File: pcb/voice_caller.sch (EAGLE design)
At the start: 28 parts, among them IC1 PRO_MICRO, IC2 AT45DB321D-S, IC3 78L12SMD, K1 TQ2SA-L2-5V

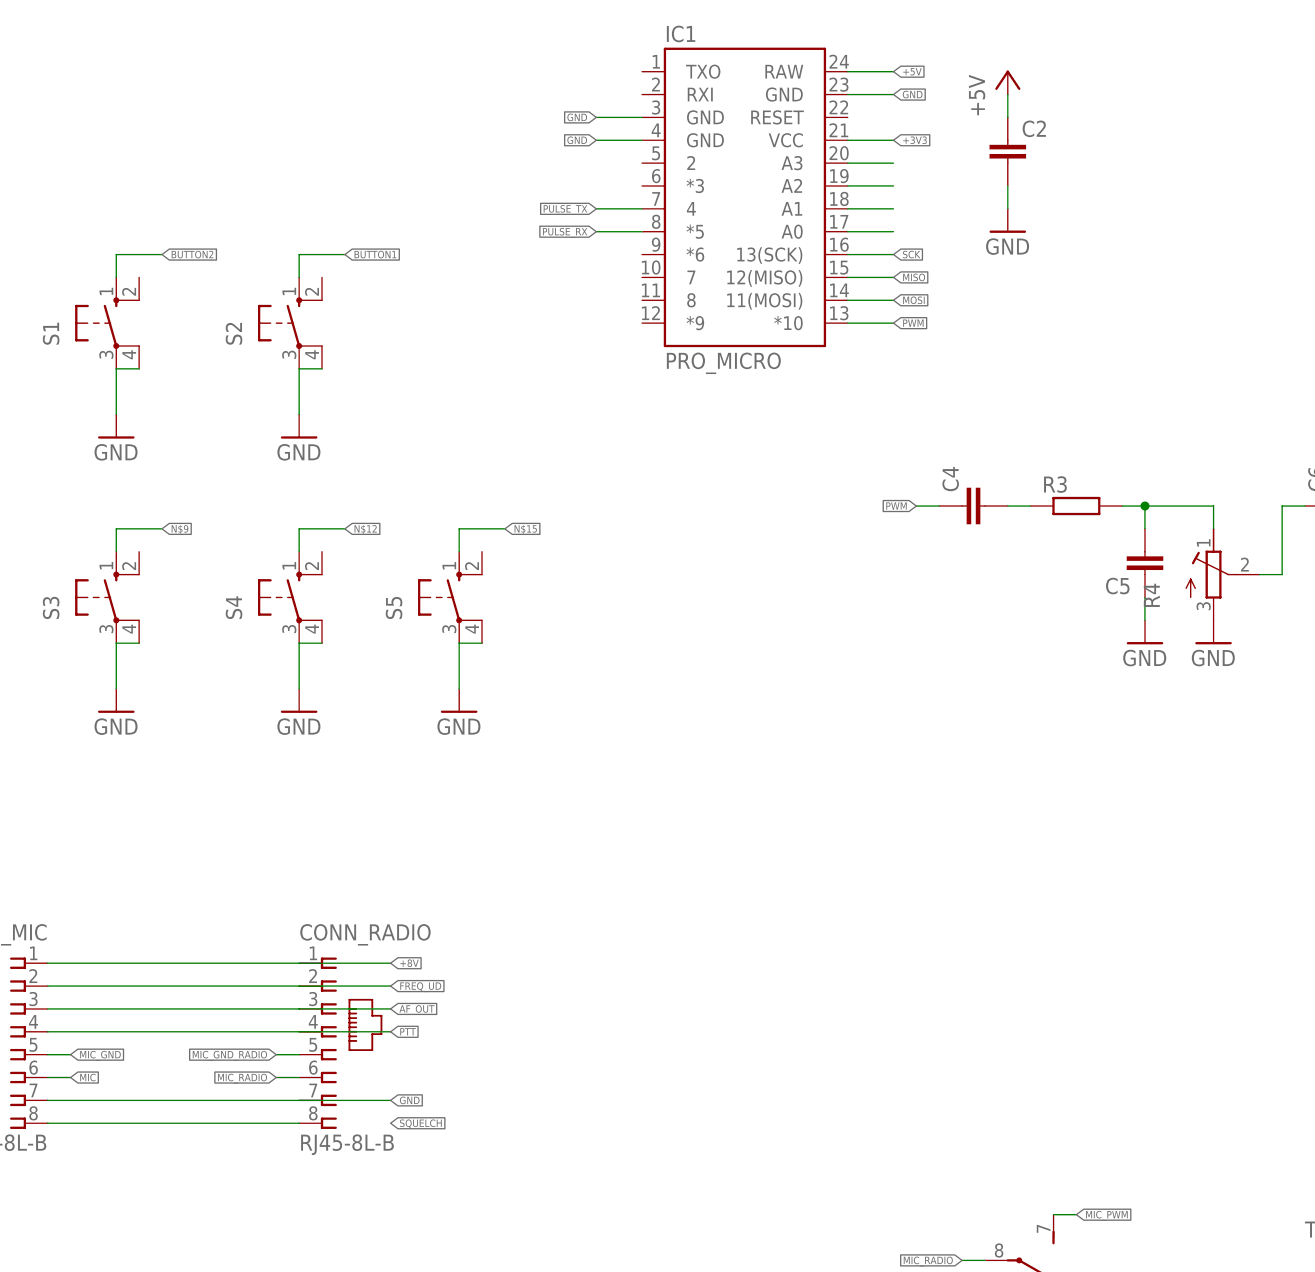
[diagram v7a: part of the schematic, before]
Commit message: PTT circuit added
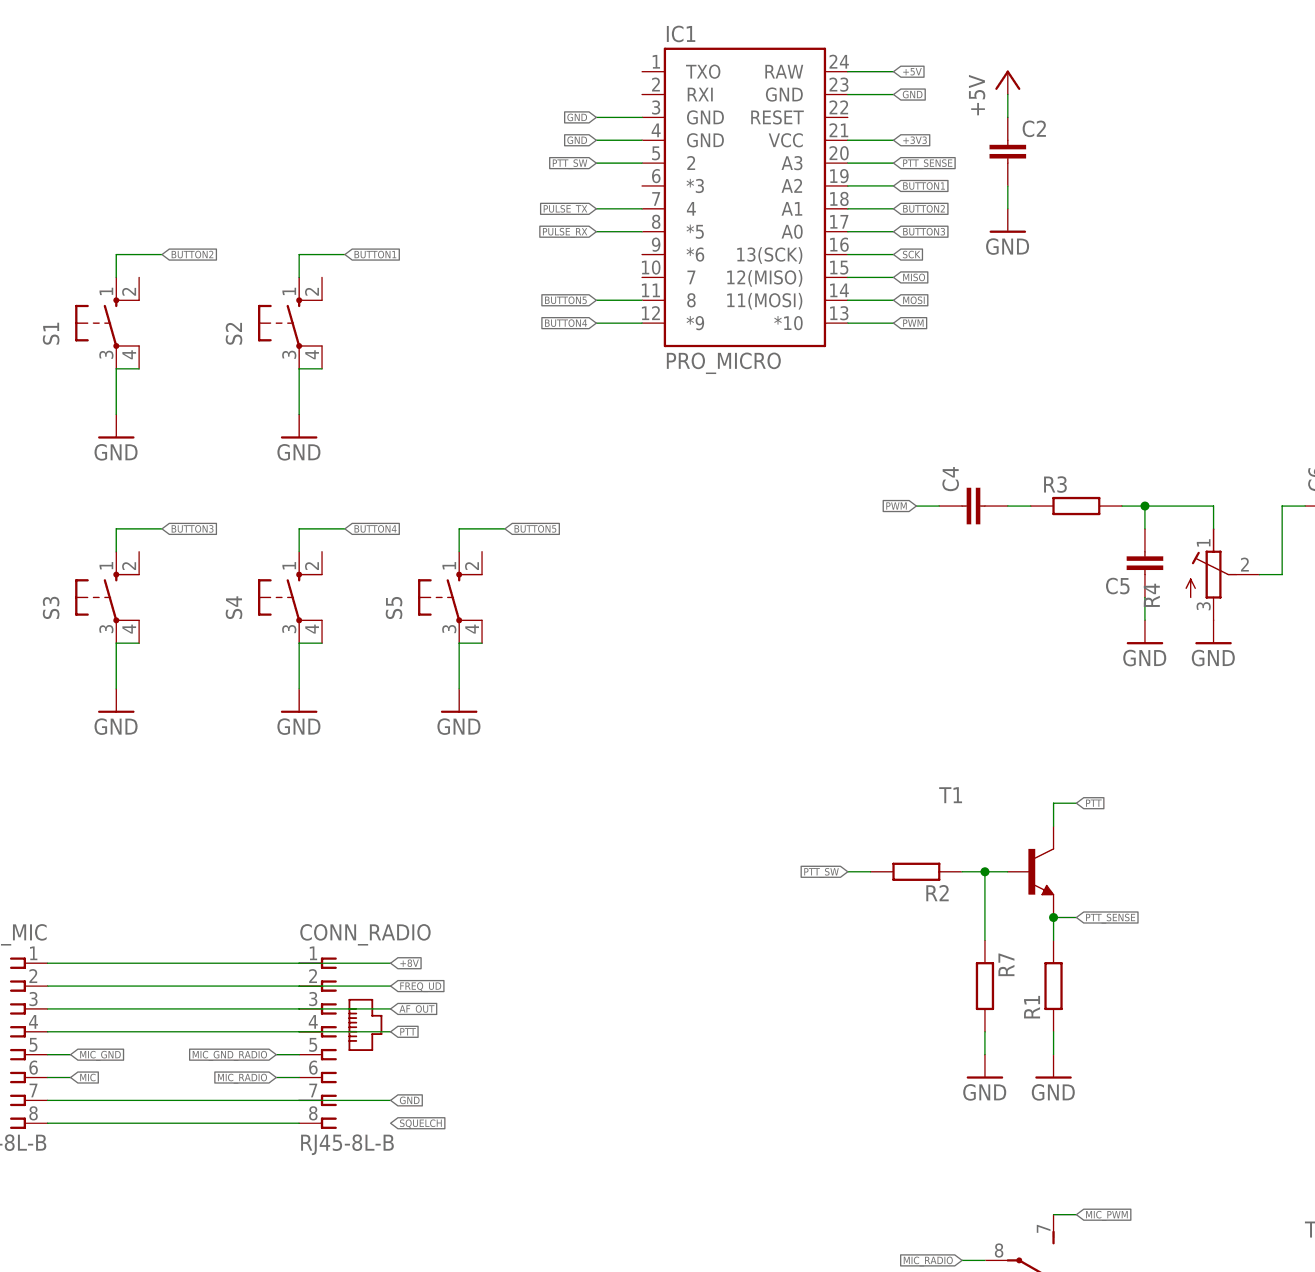
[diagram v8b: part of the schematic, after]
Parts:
- added R1, R2, R7: (no value), rcl:R-EU_M1206
- added T1: (no value), transistor:MMBT3904LT1-NPN-SOT23-BEC
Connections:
- removed net N$12: S4.S
- removed net N$15: S5.S
- removed net N$16: IC1.A1
- removed net N$17: IC1.A0
- removed net N$4: IC1.A3
- removed net N$9: S3.S
- new net BUTTON3: IC1.A0, S3.S
- new net BUTTON4: IC1.*9, S4.S
- new net BUTTON5: IC1.8, S5.S
- new net PTT_SENSE: IC1.A3, R1.2, T1.E
- new net PTT_SW: IC1.2, R2.2
- net BUTTON1: now also IC1.A2
- net BUTTON2: now also IC1.A1
- net GND: now also R1.1, R7.2
- net N$5: now also R2.1, R7.1, T1.B; no longer IC1.A2
- net PTT: now also T1.C
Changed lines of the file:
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@@
 <part name="S5" library="switch-omron" deviceset="10-XX" device=""/>
 <part name="GND17" library="supply1" deviceset="GND" device=""/>
+<part name="T1" library="transistor" deviceset="*-NPN-" device="SOT23-BEC" technology="MMBT3904LT1"/>
+<part name="R1" library="rcl" deviceset="R-EU_" device="M1206"/>
+<part name="GND18" library="supply1" deviceset="GND" device=""/>
+<part name="R2" library="rcl" deviceset="R-EU_" device="M1206"/>
+<part name="R7" library="rcl" deviceset="R-EU_" device="M1206"/>
+<part name="GND19" library="supply1" deviceset="GND" device=""/>
 </parts>
 <sheets>
@@
 <instance part="S5" gate="1" x="17.78" y="99.06"/>
 <instance part="GND17" gate="1" x="17.78" y="86.36"/>
+<instance part="T1" gate="G$1" x="81.28" y="68.58"/>
+<instance part="R1" gate="G$1" x="83.82" y="55.88" rot="R90"/>
+<instance part="GND18" gate="1" x="83.82" y="45.72"/>
+<instance part="R2" gate="G$1" x="68.58" y="68.58" rot="R180"/>
+<instance part="R7" gate="G$1" x="76.2" y="55.88" rot="R270"/>
+<instance part="GND19" gate="1" x="76.2" y="45.72"/>
 </instances>
 <busses>
@@
 <wire x1="17.78" y1="93.98" x2="20.32" y2="93.98" width="0.1524" layer="91"/>
 </segment>
+<segment>
+<pinref part="R1" gate="G$1" pin="1"/>
+<pinref part="GND18" gate="1" pin="GND"/>
+<wire x1="83.82" y1="48.26" x2="83.82" y2="50.8" width="0.1524" layer="91"/>
+</segment>
+<segment>
+<pinref part="R7" gate="G$1" pin="2"/>
+<pinref part="GND19" gate="1" pin="GND"/>
+<wire x1="76.2" y1="48.26" x2="76.2" y2="50.8" width="0.1524" layer="91"/>
+</segment>
 </net>
 <net name="MOSI" class="0">
@@
 <wire x1="0" y1="50.8" x2="10.16" y2="50.8" width="0.1524" layer="91"/>
 <label x="10.16" y="50.8" size="0.8128" layer="95" xref="yes"/>
+</segment>
+<segment>
+<pinref part="T1" gate="G$1" pin="C"/>
+<wire x1="83.82" y1="73.66" x2="83.82" y2="76.2" width="0.1524" layer="91"/>
+<wire x1="83.82" y1="76.2" x2="86.36" y2="76.2" width="0.1524" layer="91"/>
+<label x="86.36" y="76.2" size="0.8128" layer="95" xref="yes"/>
 </segment>
 </net>
@@
 <label x="-15.24" y="137.16" size="0.8128" layer="95" xref="yes"/>
 </segment>
+<segment>
+<pinref part="IC1" gate="G$1" pin="A1"/>
+<wire x1="60.96" y1="142.24" x2="66.04" y2="142.24" width="0.1524" layer="91"/>
+<label x="66.04" y="142.24" size="0.8128" layer="95" xref="yes"/>
+</segment>
 </net>
 <net name="BUTTON1" class="0">
@@
 <label x="5.08" y="137.16" size="0.8128" layer="95" xref="yes"/>
 </segment>
-</net>
-<net name="N$9" class="0">
+<segment>
+<pinref part="IC1" gate="G$1" pin="A2"/>
+<wire x1="60.96" y1="144.78" x2="66.04" y2="144.78" width="0.1524" layer="91"/>
+<label x="66.04" y="144.78" size="0.8128" layer="95" xref="yes"/>
+</segment>
+</net>
+<net name="PTT_SENSE" class="0">
+<segment>
+<pinref part="IC1" gate="G$1" pin="A3"/>
+<wire x1="60.96" y1="147.32" x2="66.04" y2="147.32" width="0.1524" layer="91"/>
+<label x="66.04" y="147.32" size="0.8128" layer="95" xref="yes"/>
+</segment>
+<segment>
+<pinref part="T1" gate="G$1" pin="E"/>
+<pinref part="R1" gate="G$1" pin="2"/>
+<wire x1="83.82" y1="60.96" x2="83.82" y2="63.5" width="0.1524" layer="91"/>
+<wire x1="83.82" y1="63.5" x2="86.36" y2="63.5" width="0.1524" layer="91"/>
+<junction x="83.82" y="63.5"/>
+<label x="86.36" y="63.5" size="0.8128" layer="95" xref="yes"/>
+</segment>
+</net>
+<net name="BUTTON3" class="0">
+<segment>
+<pinref part="IC1" gate="G$1" pin="A0"/>
+<wire x1="60.96" y1="139.7" x2="66.04" y2="139.7" width="0.1524" layer="91"/>
+<label x="66.04" y="139.7" size="0.8128" layer="95" xref="yes"/>
+</segment>
 <segment>
 <pinref part="S3" gate="1" pin="S"/>
@@
 </segment>
 </net>
-<net name="N$12" class="0">
+<net name="BUTTON5" class="0">
+<segment>
+<pinref part="IC1" gate="G$1" pin="8"/>
+<wire x1="38.1" y1="132.08" x2="33.02" y2="132.08" width="0.1524" layer="91"/>
+<label x="33.02" y="132.08" size="0.8128" layer="95" rot="R180" xref="yes"/>
+</segment>
+<segment>
+<pinref part="S5" gate="1" pin="S"/>
+<wire x1="17.78" y1="104.14" x2="17.78" y2="106.68" width="0.1524" layer="91"/>
+<wire x1="17.78" y1="106.68" x2="22.86" y2="106.68" width="0.1524" layer="91"/>
+<label x="22.86" y="106.68" size="0.8128" layer="95" xref="yes"/>
+</segment>
+</net>
+<net name="BUTTON4" class="0">
+<segment>
+<pinref part="IC1" gate="G$1" pin="*9"/>
+<wire x1="38.1" y1="129.54" x2="33.02" y2="129.54" width="0.1524" layer="91"/>
+<label x="33.02" y="129.54" size="0.8128" layer="95" rot="R180" xref="yes"/>
+</segment>
 <segment>
 <pinref part="S4" gate="1" pin="S"/>
@@
 </segment>
 </net>
-<net name="N$15" class="0">
-<segment>
-<pinref part="S5" gate="1" pin="S"/>
-<wire x1="17.78" y1="104.14" x2="17.78" y2="106.68" width="0.1524" layer="91"/>
-<wire x1="17.78" y1="106.68" x2="22.86" y2="106.68" width="0.1524" layer="91"/>
-<label x="22.86" y="106.68" size="0.8128" layer="95" xref="yes"/>
-</segment>
-</net>
-<net name="N$4" class="0">
-<segment>
-<pinref part="IC1" gate="G$1" pin="A3"/>
-<wire x1="60.96" y1="147.32" x2="66.04" y2="147.32" width="0.1524" layer="91"/>
+<net name="PTT_SW" class="0">
+<segment>
+<pinref part="IC1" gate="G$1" pin="2"/>
+<wire x1="38.1" y1="147.32" x2="33.02" y2="147.32" width="0.1524" layer="91"/>
+<label x="33.02" y="147.32" size="0.8128" layer="95" rot="R180" xref="yes"/>
+</segment>
+<segment>
+<pinref part="R2" gate="G$1" pin="2"/>
+<wire x1="63.5" y1="68.58" x2="60.96" y2="68.58" width="0.1524" layer="91"/>
+<label x="60.96" y="68.58" size="0.8128" layer="95" rot="R180" xref="yes"/>
 </segment>
 </net>
 <net name="N$5" class="0">
 <segment>
-<pinref part="IC1" gate="G$1" pin="A2"/>
-<wire x1="60.96" y1="144.78" x2="66.04" y2="144.78" width="0.1524" layer="91"/>
-</segment>
-</net>
-<net name="N$16" class="0">
-<segment>
-<pinref part="IC1" gate="G$1" pin="A1"/>
-<wire x1="60.96" y1="142.24" x2="66.04" y2="142.24" width="0.1524" layer="91"/>
-</segment>
-</net>
-<net name="N$17" class="0">
-<segment>
-<pinref part="IC1" gate="G$1" pin="A0"/>
-<wire x1="60.96" y1="139.7" x2="66.04" y2="139.7" width="0.1524" layer="91"/>
-</segment>
-</net>
+<pinref part="T1" gate="G$1" pin="B"/>
+<pinref part="R2" gate="G$1" pin="1"/>
+<wire x1="73.66" y1="68.58" x2="76.2" y2="68.58" width="0.1524" layer="91"/>
+<pinref part="R7" gate="G$1" pin="1"/>
+<wire x1="76.2" y1="68.58" x2="78.74" y2="68.58" width="0.1524" layer="91"/>
+<wire x1="76.2" y1="60.96" x2="76.2" y2="68.58" width="0.1524" layer="91"/>
+<junction x="76.2" y="68.58"/>
+</segment>
+</net>
